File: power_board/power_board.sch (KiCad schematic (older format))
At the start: 80 parts, among them J1 PROG, J10 M4, J11 5V_1, J12 M5, J13 M6, J14 M7, J15 FAN, J16 Screw_Terminal_01x02, J17 MB_interface, J18 Conn_01x02_Female, J19 12V_1, J2 M1, J20 12V_2, J21 12V_3, J22 12V_4, J23 48V_1, J24 48V_2, J25 48V_3, J26 48V_4, J27 Screw_Terminal_01x02, J3 M2, J4 Conn_01x02_Female, J5 Conn_01x02_Female, J6 Conn_01x01_Male, J7 Conn_01x01_Male, J8 Screw_Terminal_01x02, J9 M3, Q1 2N3906, SW1 SW_Push, U1 ACS758xCB-050B-PFF, U10 MAX31855KASA, U2 ACS758xCB-050B-PFF, U3 MCP2515-EST, U4 MAX31855KASA, U5 ATA6560,1, U6 BTS50085-1TMA, U7 ATmega328P-AU, U8 BTS50085-1TMA, U9 LM2596S-5, Y1 20Mhz, Y2 16Mhz

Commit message: changed board outline
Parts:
- F1, F2, F3, F4, F5, F6, F7, F8: footprint Fuse:Fuse_1206_3216Metric -> Fuse:Fuse_2920_7451Metric
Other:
- note removed: "SWAP CAN TRANSCIEVER\n\n"
- note removed: "VERIFY PIN ORDER!!!\n\n"
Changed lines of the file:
@@
 Text Notes 2150 3500 0    100  ~ 0
 Power Regulation
-Text Notes 8800 6400 0    100  ~ 20
-VERIFY PIN ORDER!!!\n\n
 $Comp
 L power:GNDREF #PWR0101
@@
 Wire Notes Line width 10 style solid
 	3950 1050 3950 2550
-Text Notes 9250 7200 0    100  ~ 20
-SWAP CAN TRANSCIEVER\n\n
 Text Notes 1100 9750 0    75   ~ 0
 Power is cut when a short is present \non J4 or J5 incating a leak.
@@
 F 0 "F1" V 14400 2450 50  0000 C CNN
 F 1 "Polyfuse_Small" V 15400 2750 50  0000 C CNN
-F 2 "Fuse:Fuse_1206_3216Metric" H 14500 2300 50  0001 L CNN
+F 2 "Fuse:Fuse_2920_7451Metric" H 14500 2300 50  0001 L CNN
 F 3 "~" H 14450 2500 50  0001 C CNN
 	1    14450 2500
@@
 F 0 "F2" V 14400 2700 50  0000 C CNN
 F 1 "Polyfuse_Small" V 15150 3000 50  0000 C CNN
-F 2 "Fuse:Fuse_1206_3216Metric" H 14500 2550 50  0001 L CNN
+F 2 "Fuse:Fuse_2920_7451Metric" H 14500 2550 50  0001 L CNN
 F 3 "~" H 14450 2750 50  0001 C CNN
 	1    14450 2750
@@
 F 0 "F3" V 14400 2950 50  0000 C CNN
 F 1 "Polyfuse_Small" V 14900 3250 50  0000 C CNN
-F 2 "Fuse:Fuse_1206_3216Metric" H 14500 2800 50  0001 L CNN
+F 2 "Fuse:Fuse_2920_7451Metric" H 14500 2800 50  0001 L CNN
 F 3 "~" H 14450 3000 50  0001 C CNN
 	1    14450 3000
@@
 F 0 "F4" V 14400 3200 50  0000 C CNN
 F 1 "Polyfuse_Small" V 14650 3500 50  0000 C CNN
-F 2 "Fuse:Fuse_1206_3216Metric" H 14500 3050 50  0001 L CNN
+F 2 "Fuse:Fuse_2920_7451Metric" H 14500 3050 50  0001 L CNN
 F 3 "~" H 14450 3250 50  0001 C CNN
 	1    14450 3250
@@
 F 0 "F5" V 15550 1650 50  0000 C CNN
 F 1 "Polyfuse_Small" V 15650 1250 50  0000 C CNN
-F 2 "Fuse:Fuse_1206_3216Metric" H 15550 1400 50  0001 L CNN
+F 2 "Fuse:Fuse_2920_7451Metric" H 15550 1400 50  0001 L CNN
 F 3 "~" H 15500 1600 50  0001 C CNN
 	1    15500 1600
@@
 F 0 "F6" V 15550 1900 50  0000 C CNN
 F 1 "Polyfuse_Small" V 15900 1500 50  0000 C CNN
-F 2 "Fuse:Fuse_1206_3216Metric" H 15550 1650 50  0001 L CNN
+F 2 "Fuse:Fuse_2920_7451Metric" H 15550 1650 50  0001 L CNN
 F 3 "~" H 15500 1850 50  0001 C CNN
 	1    15500 1850
@@
 F 0 "F7" V 15550 2150 50  0000 C CNN
 F 1 "Polyfuse_Small" V 16150 1750 50  0000 C CNN
-F 2 "Fuse:Fuse_1206_3216Metric" H 15550 1900 50  0001 L CNN
+F 2 "Fuse:Fuse_2920_7451Metric" H 15550 1900 50  0001 L CNN
 F 3 "~" H 15500 2100 50  0001 C CNN
 	1    15500 2100
@@
 F 0 "F8" V 15550 2400 50  0000 C CNN
 F 1 "Polyfuse_Small" V 16400 2000 50  0000 C CNN
-F 2 "Fuse:Fuse_1206_3216Metric" H 15550 2150 50  0001 L CNN
+F 2 "Fuse:Fuse_2920_7451Metric" H 15550 2150 50  0001 L CNN
 F 3 "~" H 15500 2350 50  0001 C CNN
 	1    15500 2350

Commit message: added new mounting holes for main board
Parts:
- added TP1: MISO, TestPoint:TestPoint_Pad_D1.0mm, symbol Connector:TestPoint
- added TP2: SCK, TestPoint:TestPoint_Pad_D1.0mm, symbol Connector:TestPoint
- added TP3: RST, TestPoint:TestPoint_Pad_D1.0mm, symbol Connector:TestPoint
- added TP4: +5V, TestPoint:TestPoint_Pad_D1.0mm, symbol Connector:TestPoint
- added TP5: MOSI, TestPoint:TestPoint_Pad_D1.0mm, symbol Connector:TestPoint
- added TP6: GND, TestPoint:TestPoint_Pad_D1.0mm, symbol Connector:TestPoint
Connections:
- wire segments 321 -> 327
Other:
- note added: "ICSP Connections\n"
- moved on the sheet: J16
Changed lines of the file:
@@
 U 1 1 5BA477AD
 P 14450 6200
-F 0 "U7" H 14600 4750 50  0000 C CNN
-F 1 "ATmega328P-AU" H 14850 4650 50  0000 C CNN
+F 0 "U7" H 13850 4750 50  0000 C CNN
+F 1 "ATmega328P-AU" H 14100 4650 50  0000 C CNN
 F 2 "Package_QFP:TQFP-32_7x7mm_P0.8mm" H 14450 6200 50  0001 C CIN
 F 3 "http://ww1.microchip.com/downloads/en/DeviceDoc/ATmega328_P%20AVR%20MCU%20with%20picoPower%20Technology%20Data%20Sheet%2040001984A.pdf" H 14450 6200 50  0001 C CNN
@@
 Microcontroller 328p\n
 Wire Notes Line width 10 style solid
-	16200 8250 13100 8250
+	16200 8500 13100 8500
 Wire Notes Line width 10 style solid
 	13100 3900 16200 3900
@@
 L Connector:Screw_Terminal_01x02 J16
 U 1 1 5BEFA5C2
-P 13100 8800
-F 0 "J16" H 13100 8900 50  0000 C CNN
-F 1 "Screw_Terminal_01x02" H 13100 9350 50  0001 C CNN
-F 2 "TerminalBlock:TerminalBlock_bornier-2_P5.08mm" H 13100 8800 50  0001 C CNN
-F 3 "~" H 13100 8800 50  0001 C CNN
-	1    13100 8800
-	1    0    0    -1
-$EndComp
-Text GLabel 12700 8900 0    50   Input ~ 0
+P 10800 9000
+F 0 "J16" H 10800 9100 50  0000 C CNN
+F 1 "Screw_Terminal_01x02" H 10800 9550 50  0001 C CNN
+F 2 "TerminalBlock:TerminalBlock_bornier-2_P5.08mm" H 10800 9000 50  0001 C CNN
+F 3 "~" H 10800 9000 50  0001 C CNN
+	1    10800 9000
+	1    0    0    -1
+$EndComp
+Text GLabel 10400 9100 0    50   Input ~ 0
 CANH
-Text GLabel 12700 8800 0    50   Input ~ 0
+Text GLabel 10400 9000 0    50   Input ~ 0
 CANL
 $Comp
@@
 	13400 2950 13550 2950
 Wire Wire Line
-	12700 8800 12900 8800
-Wire Wire Line
-	12700 8900 12900 8900
+	10400 9000 10600 9000
+Wire Wire Line
+	10400 9100 10600 9100
 $Comp
 L power:+5V #PWR0159
@@
 Wire Wire Line
 	14200 4400 14150 4400
-Wire Notes Line width 10 style solid
-	16200 3900 16200 8250
-Wire Notes Line width 10 style solid
-	13100 3900 13100 8250
 Wire Wire Line
 	9350 5250 9250 5250
@@
 	4100 4200 4400 4200
 Connection ~ 4100 4200
+$Comp
+L Connector:TestPoint TP4
+U 1 1 5BD2ED06
+P 15850 7950
+F 0 "TP4" V 15900 8000 50  0000 C CNN
+F 1 "+5V" V 15850 8200 50  0000 C CNN
+F 2 "TestPoint:TestPoint_Pad_D1.0mm" H 16050 7950 50  0001 C CNN
+F 3 "~" H 16050 7950 50  0001 C CNN
+	1    15850 7950
+	0    -1   -1   0
+$EndComp
+$Comp
+L Connector:TestPoint TP5
+U 1 1 5BD2FA15
+P 15850 8100
+F 0 "TP5" V 15900 8150 50  0000 C CNN
+F 1 "MOSI" V 15850 8350 50  0000 C CNN
+F 2 "TestPoint:TestPoint_Pad_D1.0mm" H 16050 8100 50  0001 C CNN
+F 3 "~" H 16050 8100 50  0001 C CNN
+	1    15850 8100
+	0    -1   -1   0
+$EndComp
+$Comp
+L Connector:TestPoint TP6
+U 1 1 5BD2FAD5
+P 15850 8250
+F 0 "TP6" V 15900 8300 50  0000 C CNN
+F 1 "GND" V 15850 8500 50  0000 C CNN
+F 2 "TestPoint:TestPoint_Pad_D1.0mm" H 16050 8250 50  0001 C CNN
+F 3 "~" H 16050 8250 50  0001 C CNN
+	1    15850 8250
+	0    -1   -1   0
+$EndComp
+$Comp
+L Connector:TestPoint TP1
+U 1 1 5BD4DF89
+P 15100 7950
+F 0 "TP1" V 15050 7950 50  0000 L CNN
+F 1 "MISO" V 15100 8150 50  0000 L CNN
+F 2 "TestPoint:TestPoint_Pad_D1.0mm" H 15300 7950 50  0001 C CNN
+F 3 "~" H 15300 7950 50  0001 C CNN
+	1    15100 7950
+	0    1    1    0
+$EndComp
+$Comp
+L Connector:TestPoint TP2
+U 1 1 5BD4E101
+P 15100 8100
+F 0 "TP2" V 15050 8100 50  0000 L CNN
+F 1 "SCK" V 15100 8300 50  0000 L CNN
+F 2 "TestPoint:TestPoint_Pad_D1.0mm" H 15300 8100 50  0001 C CNN
+F 3 "~" H 15300 8100 50  0001 C CNN
+	1    15100 8100
+	0    1    1    0
+$EndComp
+$Comp
+L Connector:TestPoint TP3
+U 1 1 5BD4E1BB
+P 15100 8250
+F 0 "TP3" V 15050 8250 50  0000 L CNN
+F 1 "RST" V 15100 8450 50  0000 L CNN
+F 2 "TestPoint:TestPoint_Pad_D1.0mm" H 15300 8250 50  0001 C CNN
+F 3 "~" H 15300 8250 50  0001 C CNN
+	1    15100 8250
+	0    1    1    0
+$EndComp
+$Comp
+L power:GNDREF #PWR0154
+U 1 1 5BE45069
+P 15950 8250
+F 0 "#PWR0154" H 15950 8000 50  0001 C CNN
+F 1 "GNDREF" H 15955 8077 50  0000 C CNN
+F 2 "" H 15950 8250 50  0001 C CNN
+F 3 "" H 15950 8250 50  0001 C CNN
+	1    15950 8250
+	1    0    0    -1
+$EndComp
+$Comp
+L power:VPP #PWR0167
+U 1 1 5BE633DD
+P 15950 7950
+F 0 "#PWR0167" H 15950 7800 50  0001 C CNN
+F 1 "VPP" H 15965 8123 50  0000 C CNN
+F 2 "" H 15950 7950 50  0001 C CNN
+F 3 "" H 15950 7950 50  0001 C CNN
+	1    15950 7950
+	1    0    0    -1
+$EndComp
+Wire Notes Line width 10 style solid
+	13100 3900 13100 8500
+Wire Notes Line width 10 style solid
+	16200 3900 16200 8500
+Text GLabel 15900 8100 2    50   Input ~ 0
+MOSI
+Text GLabel 15050 8100 0    50   Input ~ 0
+SCK
+Text GLabel 15050 7950 0    50   Input ~ 0
+MISO
+Text GLabel 15050 8250 0    50   Input ~ 0
+RESET
+Wire Wire Line
+	15850 7950 15950 7950
+Wire Wire Line
+	15850 8100 15900 8100
+Wire Wire Line
+	15850 8250 15950 8250
+Wire Wire Line
+	15050 7950 15100 7950
+Wire Wire Line
+	15050 8100 15100 8100
+Wire Wire Line
+	15050 8250 15100 8250
+Text Notes 14850 7800 0    75   ~ 0
+ICSP Connections\n
 $EndSCHEMATC

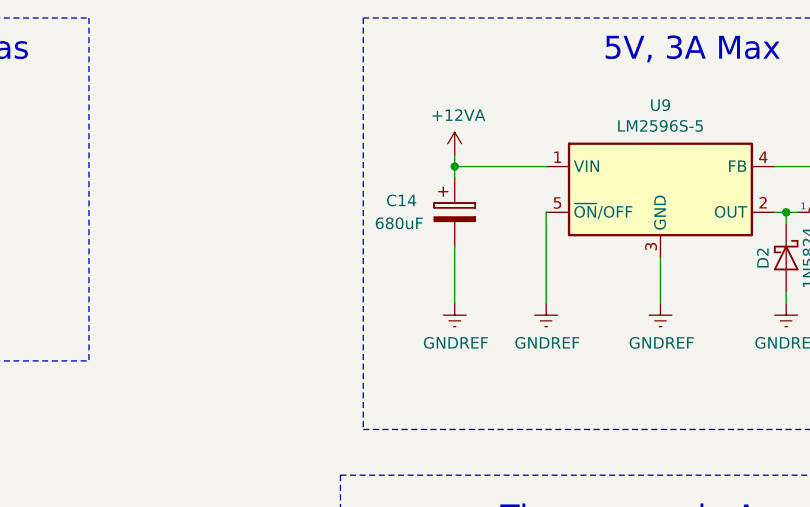
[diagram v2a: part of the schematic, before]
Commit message: Changed 5v input capacitor package
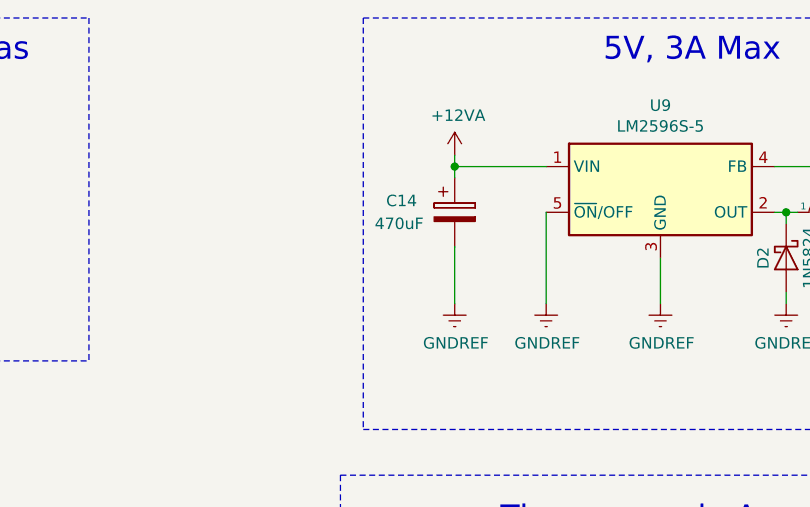
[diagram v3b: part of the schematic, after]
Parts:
- C14: value 680uF -> 470uF; footprint Capacitor_THT:CP_Radial_D7.5mm_P2.50mm -> Capacitor_THT:CP_Radial_D8.0mm_P5.00mm
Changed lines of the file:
@@
 P 5550 1900
 F 0 "C14" H 5250 1950 50  0000 L CNN
-F 1 "680uF" H 5200 1850 50  0000 L CNN
-F 2 "Capacitor_THT:CP_Radial_D7.5mm_P2.50mm" H 5588 1750 50  0001 C CNN
+F 1 "470uF" H 5200 1850 50  0000 L CNN
+F 2 "Capacitor_THT:CP_Radial_D8.0mm_P5.00mm" H 5588 1750 50  0001 C CNN
 F 3 "~" H 5550 1900 50  0001 C CNN
 	1    5550 1900

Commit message: Updated D2 package
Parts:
- D2: footprint Diode_SMD:D_SMB -> Diode_SMD:D_SMC
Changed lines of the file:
@@
 Sheet 1 1
 Title "Power Board"
-Date "2018-09-20"
-Rev "1.1.1"
+Date "2018-10-29"
+Rev "1.0.0"
 Comp "Missouri University of Science and Technology"
 Comment1 "PCB for the ROV's Power System"
@@
 F 0 "D2" H 7000 2000 50  0000 C CNN
 F 1 "1N5824" H 7000 2200 50  0000 C CNN
-F 2 "Diode_SMD:D_SMB" H 7000 2100 50  0001 C CNN
+F 2 "Diode_SMD:D_SMC" H 7000 2100 50  0001 C CNN
 F 3 "~" H 7000 2100 50  0001 C CNN
 	1    7000 2100

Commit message: S1.0.0 B1.0.1 Update silkscreen for schematic/pcb version
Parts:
- U5: symbol URT_cache:ATA6560,1 -> power_board-rescue:ATA6560,1-URT_cache
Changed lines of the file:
@@
 	4550 8550 4550 8750
 $Comp
-L URT_cache:ATA6560,1 U5
+L power_board-rescue:ATA6560,1-URT_cache U5
 U 1 1 5BCC7310
 P 10150 8350

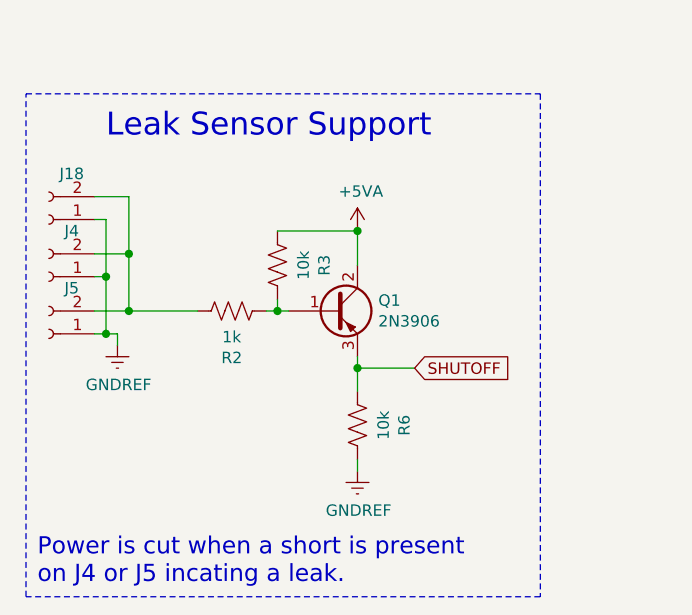
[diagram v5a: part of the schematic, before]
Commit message: Fixed water ingress shutoff signal control
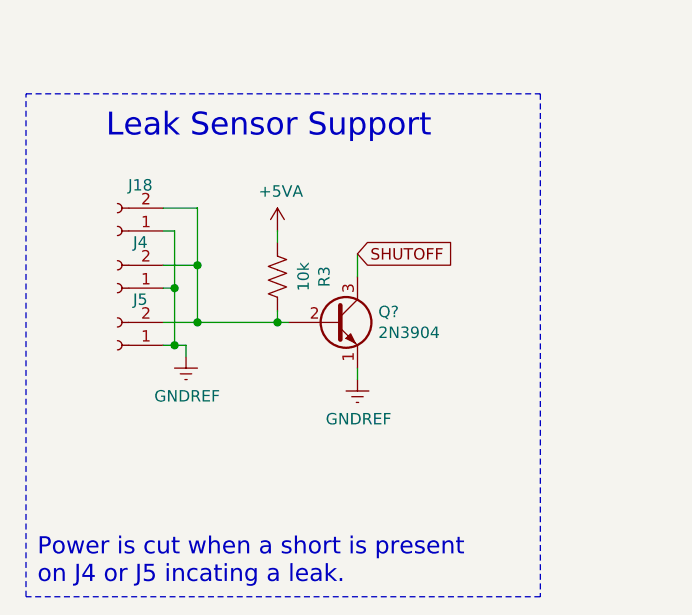
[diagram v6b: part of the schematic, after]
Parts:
- removed Q1: 2N3906, Package_TO_SOT_SMD:SOT-23, symbol Device:Q_PNP_BCE
- removed R2: 1k, Resistor_SMD:R_0603_1608Metric, symbol Device:R_US
- removed R6: 10k, Resistor_SMD:R_0603_1608Metric, symbol Device:R_US
- added Q?: 2N3904, Package_TO_SOT_THT:TO-92_Inline, symbol Transistor_BJT:2N3904
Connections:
- net GNDREF: now also Q?.1 (E)
- net SHUTOFF: now also Q?.3 (C)
- net at J18.2 (Pin_2), J4.2 (Pin_2), J5.2 (Pin_2): now also R3.1, Q?.2 (B)
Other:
- moved on the sheet: J18, J4, J5, R3
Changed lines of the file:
@@
 L Connector:Conn_01x02_Female J4
 U 1 1 5BA58C27
-P 1150 8400
-F 0 "J4" H 1050 8200 50  0000 C CNN
-F 1 "Conn_01x02_Female" H 1044 8166 50  0001 C CNN
-F 2 "Connector_JST:JST_GH_BM02B-GHS-TBT_1x02-1MP_P1.25mm_Vertical" H 1150 8400 50  0001 C CNN
-F 3 "~" H 1150 8400 50  0001 C CNN
-	1    1150 8400
+P 1450 8450
+F 0 "J4" H 1350 8250 50  0000 C CNN
+F 1 "Conn_01x02_Female" H 1344 8216 50  0001 C CNN
+F 2 "Connector_JST:JST_GH_BM02B-GHS-TBT_1x02-1MP_P1.25mm_Vertical" H 1450 8450 50  0001 C CNN
+F 3 "~" H 1450 8450 50  0001 C CNN
+	1    1450 8450
 	-1   0    0    1
 $EndComp
@@
 L Connector:Conn_01x02_Female J5
 U 1 1 5BA58C75
-P 1150 8650
-F 0 "J5" H 1050 8450 50  0000 C CNN
-F 1 "Conn_01x02_Female" H 1044 8416 50  0001 C CNN
-F 2 "Connector_JST:JST_GH_BM02B-GHS-TBT_1x02-1MP_P1.25mm_Vertical" H 1150 8650 50  0001 C CNN
-F 3 "~" H 1150 8650 50  0001 C CNN
-	1    1150 8650
+P 1450 8700
+F 0 "J5" H 1350 8500 50  0000 C CNN
+F 1 "Conn_01x02_Female" H 1344 8466 50  0001 C CNN
+F 2 "Connector_JST:JST_GH_BM02B-GHS-TBT_1x02-1MP_P1.25mm_Vertical" H 1450 8700 50  0001 C CNN
+F 3 "~" H 1450 8700 50  0001 C CNN
+	1    1450 8700
 	-1   0    0    1
 $EndComp
@@
 L power:GNDREF #PWR0122
 U 1 1 5BA59056
-P 1450 8700
-F 0 "#PWR0122" H 1450 8450 50  0001 C CNN
-F 1 "GNDREF" H 1455 8527 50  0000 C CNN
-F 2 "" H 1450 8700 50  0001 C CNN
-F 3 "" H 1450 8700 50  0001 C CNN
-	1    1450 8700
-	1    0    0    -1
-$EndComp
-Wire Wire Line
-	1350 8650 1400 8650
-Wire Wire Line
-	1450 8650 1450 8700
+P 1750 8750
+F 0 "#PWR0122" H 1750 8500 50  0001 C CNN
+F 1 "GNDREF" H 1755 8577 50  0000 C CNN
+F 2 "" H 1750 8750 50  0001 C CNN
+F 3 "" H 1750 8750 50  0001 C CNN
+	1    1750 8750
+	1    0    0    -1
+$EndComp
+Wire Wire Line
+	1650 8700 1700 8700
+Wire Wire Line
+	1750 8700 1750 8750
 Text Notes 1400 7800 0    100  ~ 0
 Leak Sensor Support
@@
 	1    0    0    -1
 $EndComp
-Text GLabel 2750 8800 2    50   Input ~ 0
+Text GLabel 2500 8300 2    50   Input ~ 0
 SHUTOFF
 $Comp
@@
 	2850 4800 2850 4950
 $Comp
-L Device:Q_PNP_BCE Q1
-U 1 1 5BCD011E
-P 2400 8550
-F 0 "Q1" H 2591 8596 50  0000 L CNN
-F 1 "2N3906" H 2591 8505 50  0000 L CNN
-F 2 "Package_TO_SOT_SMD:SOT-23" H 2600 8650 50  0001 C CNN
-F 3 "~" H 2400 8550 50  0001 C CNN
-	1    2400 8550
-	1    0    0    -1
-$EndComp
-$Comp
-L Device:R_US R6
-U 1 1 5BCF4520
-P 2500 9050
-F 0 "R6" V 2295 9050 50  0000 C CNN
-F 1 "10k" V 2386 9050 50  0000 C CNN
-F 2 "Resistor_SMD:R_0603_1608Metric" V 2540 9040 50  0001 C CNN
-F 3 "~" H 2500 9050 50  0001 C CNN
-	1    2500 9050
-	-1   0    0    1
-$EndComp
-$Comp
-L Device:R_US R2
-U 1 1 5BCF4727
-P 1950 8550
-F 0 "R2" V 1745 8550 50  0000 C CNN
-F 1 "1k" V 1836 8550 50  0000 C CNN
-F 2 "Resistor_SMD:R_0603_1608Metric" V 1990 8540 50  0001 C CNN
-F 3 "~" H 1950 8550 50  0001 C CNN
-	1    1950 8550
-	0    -1   -1   0
-$EndComp
-$Comp
 L power:+5VA #PWR0103
 U 1 1 5BCF4A60
-P 2500 8200
-F 0 "#PWR0103" H 2500 8050 50  0001 C CNN
-F 1 "+5VA" H 2515 8373 50  0000 C CNN
-F 2 "" H 2500 8200 50  0001 C CNN
-F 3 "" H 2500 8200 50  0001 C CNN
-	1    2500 8200
+P 2150 8200
+F 0 "#PWR0103" H 2150 8050 50  0001 C CNN
+F 1 "+5VA" H 2165 8373 50  0000 C CNN
+F 2 "" H 2150 8200 50  0001 C CNN
+F 3 "" H 2150 8200 50  0001 C CNN
+	1    2150 8200
 	1    0    0    -1
 $EndComp
@@
 L Device:R_US R3
 U 1 1 5BCF4C45
-P 2150 8350
-F 0 "R3" V 1945 8350 50  0000 C CNN
-F 1 "10k" V 2036 8350 50  0000 C CNN
-F 2 "Resistor_SMD:R_0603_1608Metric" V 2190 8340 50  0001 C CNN
-F 3 "~" H 2150 8350 50  0001 C CNN
-	1    2150 8350
+P 2150 8400
+F 0 "R3" V 1945 8400 50  0000 C CNN
+F 1 "10k" V 2036 8400 50  0000 C CNN
+F 2 "Resistor_SMD:R_0603_1608Metric" V 2190 8390 50  0001 C CNN
+F 3 "~" H 2150 8400 50  0001 C CNN
+	1    2150 8400
 	-1   0    0    1
 $EndComp
 Wire Wire Line
-	2500 8350 2500 8200
-Wire Wire Line
-	2500 8200 2150 8200
-Connection ~ 2500 8200
-Wire Wire Line
-	2100 8550 2150 8550
-Wire Wire Line
-	2150 8500 2150 8550
-Connection ~ 2150 8550
-Wire Wire Line
-	2150 8550 2200 8550
+	2150 8550 2150 8600
+Connection ~ 2150 8600
+Wire Wire Line
+	2150 8600 2200 8600
 $Comp
 L power:GNDREF #PWR0104
 U 1 1 5BD31EDE
-P 2500 9250
-F 0 "#PWR0104" H 2500 9000 50  0001 C CNN
-F 1 "GNDREF" H 2505 9077 50  0000 C CNN
-F 2 "" H 2500 9250 50  0001 C CNN
-F 3 "" H 2500 9250 50  0001 C CNN
-	1    2500 9250
-	1    0    0    -1
-$EndComp
-Wire Wire Line
-	2500 9250 2500 9200
-Wire Wire Line
-	2500 8750 2500 8800
-Wire Wire Line
-	2750 8800 2500 8800
-Connection ~ 2500 8800
-Wire Wire Line
-	2500 8800 2500 8900
+P 2500 8850
+F 0 "#PWR0104" H 2500 8600 50  0001 C CNN
+F 1 "GNDREF" H 2505 8677 50  0000 C CNN
+F 2 "" H 2500 8850 50  0001 C CNN
+F 3 "" H 2500 8850 50  0001 C CNN
+	1    2500 8850
+	1    0    0    -1
+$EndComp
 Text GLabel 1500 4550 0    50   Input ~ 0
 SHUTOFF
@@
 	2000 4100 2000 4150
 Wire Wire Line
-	1350 8550 1500 8550
+	1650 8600 1800 8600
 $Comp
 L Connector:Conn_01x02_Female J18
 U 1 1 5BC10D2D
-P 1150 8150
-F 0 "J18" H 1050 7950 50  0000 C CNN
-F 1 "Conn_01x02_Female" H 1044 7916 50  0001 C CNN
-F 2 "Connector_JST:JST_GH_BM02B-GHS-TBT_1x02-1MP_P1.25mm_Vertical" H 1150 8150 50  0001 C CNN
-F 3 "~" H 1150 8150 50  0001 C CNN
-	1    1150 8150
+P 1450 8200
+F 0 "J18" H 1350 8000 50  0000 C CNN
+F 1 "Conn_01x02_Female" H 1344 7966 50  0001 C CNN
+F 2 "Connector_JST:JST_GH_BM02B-GHS-TBT_1x02-1MP_P1.25mm_Vertical" H 1450 8200 50  0001 C CNN
+F 3 "~" H 1450 8200 50  0001 C CNN
+	1    1450 8200
 	-1   0    0    1
 $EndComp
 Wire Wire Line
-	1350 8300 1500 8300
-Wire Wire Line
-	1500 8300 1500 8550
-Connection ~ 1500 8550
-Wire Wire Line
-	1500 8550 1800 8550
-Wire Wire Line
-	1350 8050 1500 8050
-Wire Wire Line
-	1500 8050 1500 8300
-Connection ~ 1500 8300
-Wire Wire Line
-	1350 8150 1400 8150
-Wire Wire Line
-	1400 8150 1400 8400
-Connection ~ 1400 8650
-Wire Wire Line
-	1400 8650 1450 8650
-Wire Wire Line
-	1350 8400 1400 8400
-Connection ~ 1400 8400
-Wire Wire Line
-	1400 8400 1400 8650
+	1650 8350 1800 8350
+Wire Wire Line
+	1800 8350 1800 8600
+Connection ~ 1800 8600
+Wire Wire Line
+	1650 8100 1800 8100
+Wire Wire Line
+	1800 8100 1800 8350
+Connection ~ 1800 8350
+Wire Wire Line
+	1650 8200 1700 8200
+Wire Wire Line
+	1700 8200 1700 8450
+Connection ~ 1700 8700
+Wire Wire Line
+	1700 8700 1750 8700
+Wire Wire Line
+	1650 8450 1700 8450
+Connection ~ 1700 8450
+Wire Wire Line
+	1700 8450 1700 8700
 Wire Wire Line
 	15350 5800 15600 5800
@@
 Text Notes 14850 7800 0    75   ~ 0
 ICSP Connections\n
+$Comp
+L Transistor_BJT:2N3904 Q?
+U 1 1 5BF7B85C
+P 2400 8600
+F 0 "Q?" H 2591 8646 50  0000 L CNN
+F 1 "2N3904" H 2591 8555 50  0000 L CNN
+F 2 "Package_TO_SOT_THT:TO-92_Inline" H 2600 8525 50  0001 L CIN
+F 3 "https://www.fairchildsemi.com/datasheets/2N/2N3904.pdf" H 2400 8600 50  0001 L CNN
+	1    2400 8600
+	1    0    0    -1
+$EndComp
+Wire Wire Line
+	2150 8200 2150 8250
+Wire Wire Line
+	2500 8400 2500 8300
+Wire Wire Line
+	2500 8800 2500 8850
+Wire Wire Line
+	1800 8600 2150 8600
 $EndSCHEMATC
